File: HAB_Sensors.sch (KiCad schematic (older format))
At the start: 17 parts, among them U6 MCP9808T, U7 BME280, U8 LM4030, U9 LSM9DS1

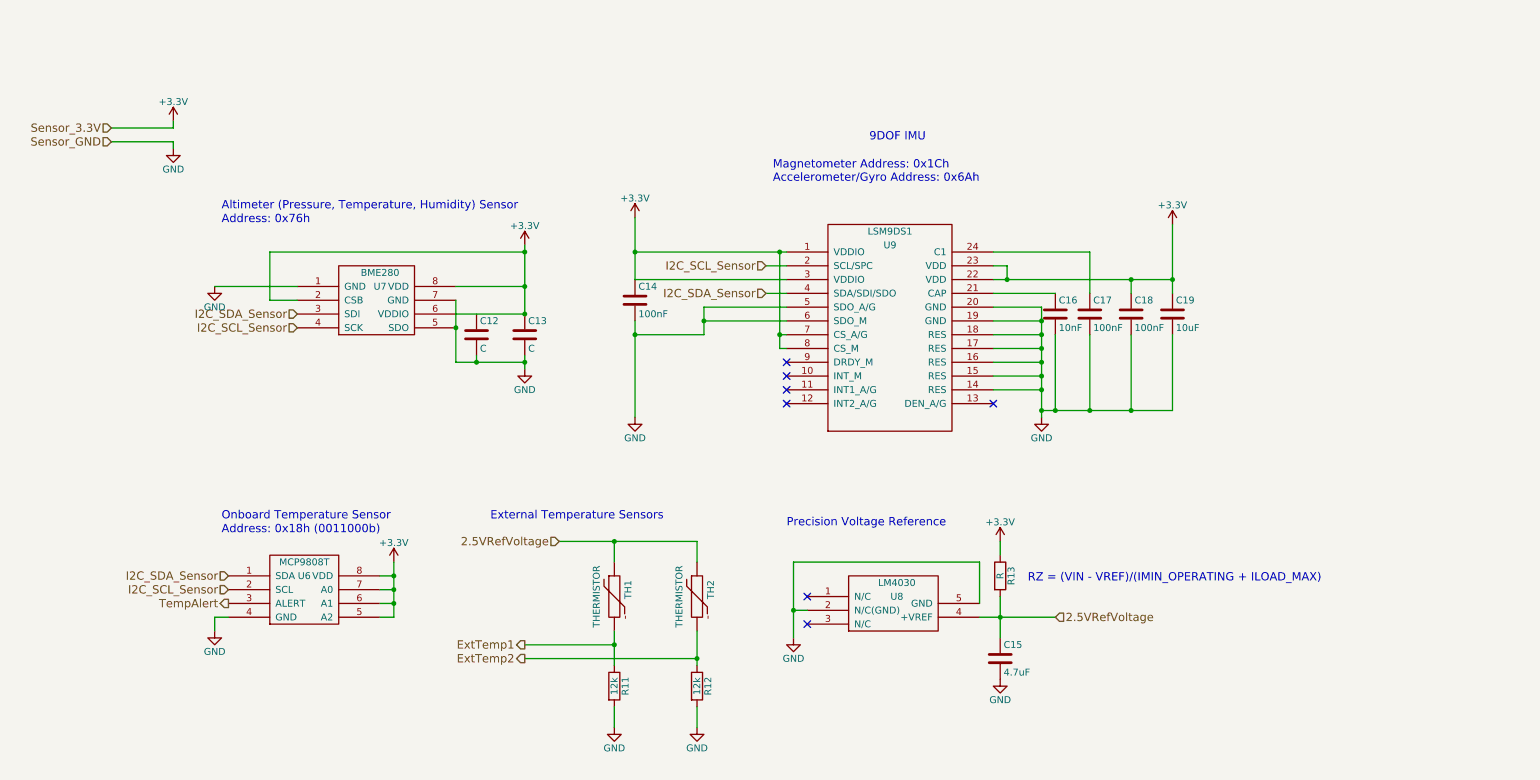
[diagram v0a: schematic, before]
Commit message: added add'l temperature sensor
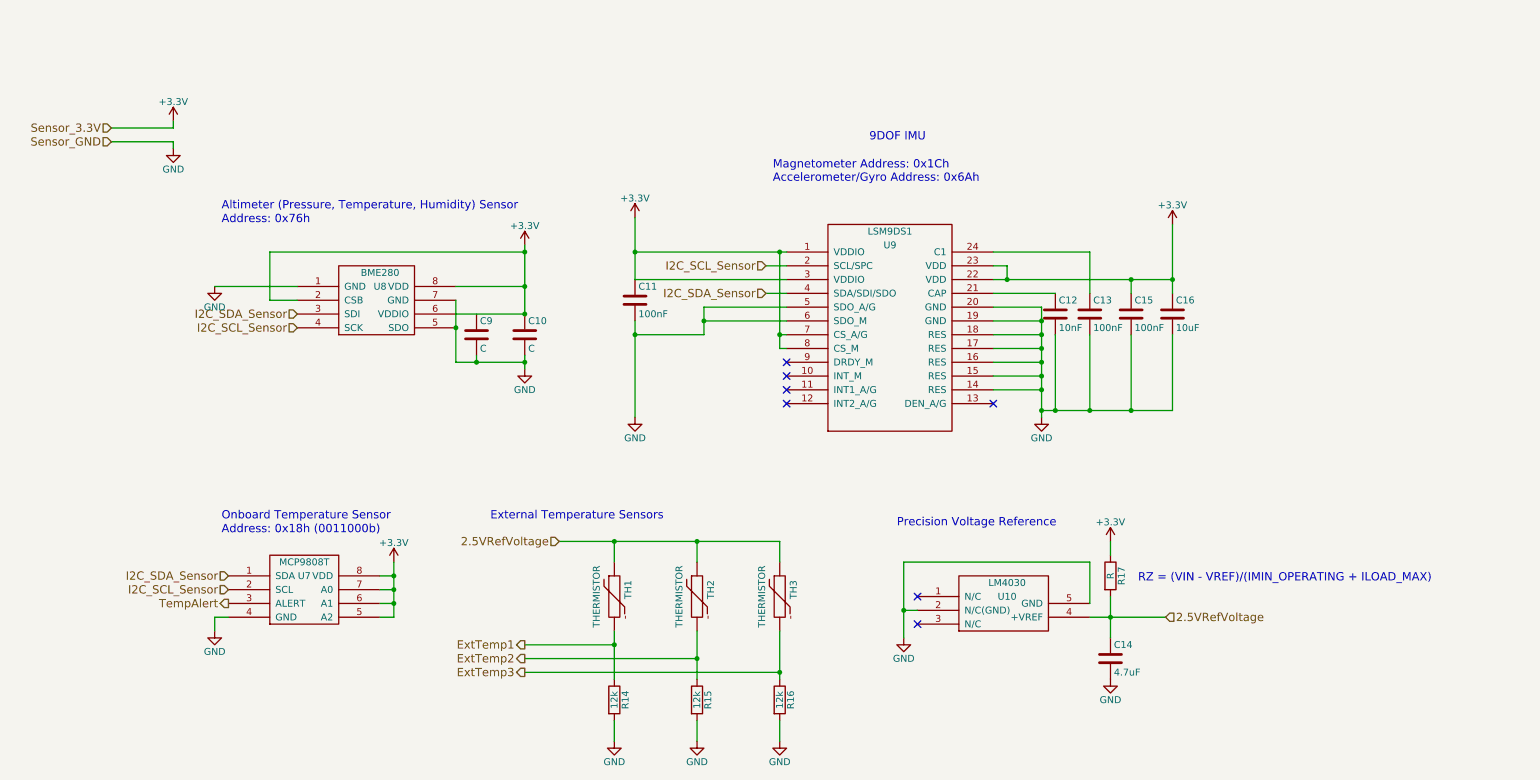
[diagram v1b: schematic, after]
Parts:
- added R15: 12k, symbol R
- added TH3: THERMISTOR, symbol THERMISTOR
- renumbered C13 to C10, C14 to C11, C16 to C12, C17 to C13, C15 to C14, C18 to C15, C19 to C16, C12 to C9, R11 to R14, R12 to R16, R13 to R17, U8 to U10, U6 to U7, U7 to U8
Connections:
- net 2.5VRefVoltage: now also TH3.1
- net ExtTemp2: now also R15.1; no longer R16.1
- net GND: now also R15.2
- new net ExtTemp3: R16.1, TH3.2
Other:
- moved on the sheet: C14, R14, R16, R17, U10

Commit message: Schematics updated/components generated/PCB started
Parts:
- C10, C11, C12, C13, C14, C15, C16, C9: footprint (none) -> Capacitors_SMD:C_0603
- R14, R15, R16, R17: footprint (none) -> Resistors_SMD:R_0603
- TH1, TH2, TH3: footprint (none) -> Connect:PINHEAD1-2
- U10: footprint MODULE -> TO_SOT_Packages_SMD:SOT-23-5
- U7: footprint MODULE -> Housings_SSOP:MSOP-8_3x3mm_Pitch0.65mm
- U8: footprint MODULE -> SPEX_Parts:LGA-8
- U9: footprint MODULE -> SPEX_Parts:LGA-24
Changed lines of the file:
@@
 LIBS:parts
 LIBS:PRESSURE-BMP180_LGA7_
+LIBS:74xgxx
+LIBS:ac-dc
+LIBS:actel
+LIBS:Altera
+LIBS:analog_devices
+LIBS:brooktre
+LIBS:cmos_ieee
+LIBS:dc-dc
+LIBS:diode
+LIBS:elec-unifil
+LIBS:ESD_Protection
+LIBS:ftdi
+LIBS:gennum
+LIBS:graphic
+LIBS:hc11
+LIBS:ir
+LIBS:Lattice
+LIBS:logo
+LIBS:maxim
+LIBS:microchip_dspic33dsc
+LIBS:microchip_pic10mcu
+LIBS:microchip_pic12mcu
+LIBS:microchip_pic16mcu
+LIBS:microchip_pic18mcu
+LIBS:microchip_pic32mcu
+LIBS:motor_drivers
+LIBS:msp430
+LIBS:nordicsemi
+LIBS:nxp_armmcu
+LIBS:onsemi
+LIBS:Oscillators
+LIBS:Power_Management
+LIBS:powerint
+LIBS:pspice
+LIBS:references
+LIBS:relays
+LIBS:rfcom
+LIBS:sensors
+LIBS:silabs
+LIBS:stm8
+LIBS:stm32
+LIBS:supertex
+LIBS:switches
+LIBS:transf
+LIBS:ttl_ieee
+LIBS:video
+LIBS:Xicor
+LIBS:Zilog
 LIBS:Spex-Mainboard-Hardware-cache
 EELAYER 25 0
@@
 F 0 "U9" H 6900 3100 50  0000 C CNN
 F 1 "LSM9DS1" H 6900 3200 50  0000 C CNN
-F 2 "MODULE" H 7050 1800 50  0001 C CNN
+F 2 "SPEX_Parts:LGA-24" H 7050 1800 50  0001 C CNN
 F 3 "DOCUMENTATION" H 7050 1800 50  0001 C CNN
 	1    6900 2500
@@
 F 0 "U7" H 2650 4600 50  0000 C CNN
 F 1 "MCP9808T" H 2650 4700 50  0000 C CNN
-F 2 "MODULE" H 2750 3950 50  0001 C CNN
+F 2 "Housings_SSOP:MSOP-8_3x3mm_Pitch0.65mm" H 2750 3950 50  0001 C CNN
 F 3 "DOCUMENTATION" H 2600 4050 50  0001 C CNN
 	1    2450 4450
@@
 F 0 "U8" H 3200 2500 50  0000 C CNN
 F 1 "BME280" H 3200 2600 50  0000 C CNN
-F 2 "MODULE" H 3300 1950 50  0001 C CNN
+F 2 "SPEX_Parts:LGA-8" H 3300 1950 50  0001 C CNN
 F 3 "DOCUMENTATION" H 3150 2050 50  0001 C CNN
 	1    3000 2350
@@
 $EndComp
 $Comp
-L +3.3V #PWR032
+L +3.3V #PWR036
 U 1 1 56DF3EDE
 P 4250 1900
-F 0 "#PWR032" H 4250 1750 50  0001 C CNN
+F 0 "#PWR036" H 4250 1750 50  0001 C CNN
 F 1 "+3.3V" H 4250 2040 50  0000 C CNN
 F 2 "" H 4250 1900 50  0000 C CNN
@@
 $EndComp
 $Comp
-L +3.3V #PWR033
+L +3.3V #PWR037
 U 1 1 56DF3EFC
 P 3300 4200
-F 0 "#PWR033" H 3300 4050 50  0001 C CNN
+F 0 "#PWR037" H 3300 4050 50  0001 C CNN
 F 1 "+3.3V" H 3300 4340 50  0000 C CNN
 F 2 "" H 3300 4200 50  0000 C CNN
@@
 $EndComp
 $Comp
-L +3.3V #PWR034
+L +3.3V #PWR038
 U 1 1 56DF3F1A
 P 8950 1750
-F 0 "#PWR034" H 8950 1600 50  0001 C CNN
+F 0 "#PWR038" H 8950 1600 50  0001 C CNN
 F 1 "+3.3V" H 8950 1890 50  0000 C CNN
 F 2 "" H 8950 1750 50  0000 C CNN
@@
 $EndComp
 $Comp
-L +3.3V #PWR035
+L +3.3V #PWR039
 U 1 1 56DF3F56
 P 5050 1700
-F 0 "#PWR035" H 5050 1550 50  0001 C CNN
+F 0 "#PWR039" H 5050 1550 50  0001 C CNN
 F 1 "+3.3V" H 5050 1840 50  0000 C CNN
 F 2 "" H 5050 1700 50  0000 C CNN
@@
 $EndComp
 $Comp
-L GND #PWR036
+L GND #PWR040
 U 1 1 56DF3F74
 P 4250 2800
-F 0 "#PWR036" H 4250 2550 50  0001 C CNN
+F 0 "#PWR040" H 4250 2550 50  0001 C CNN
 F 1 "GND" H 4250 2650 50  0000 C CNN
 F 2 "" H 4250 2800 50  0000 C CNN
@@
 $EndComp
 $Comp
-L GND #PWR037
+L GND #PWR041
 U 1 1 56DF3F92
 P 2000 2200
-F 0 "#PWR037" H 2000 1950 50  0001 C CNN
+F 0 "#PWR041" H 2000 1950 50  0001 C CNN
 F 1 "GND" H 2000 2050 50  0000 C CNN
 F 2 "" H 2000 2200 50  0000 C CNN
@@
 $EndComp
 $Comp
-L GND #PWR038
+L GND #PWR042
 U 1 1 56DF3FCE
 P 2000 4700
-F 0 "#PWR038" H 2000 4450 50  0001 C CNN
+F 0 "#PWR042" H 2000 4450 50  0001 C CNN
 F 1 "GND" H 2000 4550 50  0000 C CNN
 F 2 "" H 2000 4700 50  0000 C CNN
@@
 $EndComp
 $Comp
-L GND #PWR039
+L GND #PWR043
 U 1 1 56DF3FEC
 P 8000 3150
-F 0 "#PWR039" H 8000 2900 50  0001 C CNN
+F 0 "#PWR043" H 8000 2900 50  0001 C CNN
 F 1 "GND" H 8000 3000 50  0000 C CNN
 F 2 "" H 8000 3150 50  0000 C CNN
@@
 F 0 "C10" H 4275 2650 50  0000 L CNN
 F 1 "C" H 4275 2450 50  0000 L CNN
-F 2 "" H 4288 2400 50  0000 C CNN
+F 2 "Capacitors_SMD:C_0603" H 4288 2400 50  0001 C CNN
 F 3 "" H 4250 2550 50  0000 C CNN
 	1    4250 2550
@@
 F 0 "C9" H 3925 2650 50  0000 L CNN
 F 1 "C" H 3925 2450 50  0000 L CNN
-F 2 "" H 3938 2400 50  0000 C CNN
+F 2 "Capacitors_SMD:C_0603" H 3938 2400 50  0001 C CNN
 F 3 "" H 3900 2550 50  0000 C CNN
 	1    3900 2550
@@
 F 0 "C11" H 5075 2400 50  0000 L CNN
 F 1 "100nF" H 5075 2200 50  0000 L CNN
-F 2 "" H 5088 2150 50  0000 C CNN
+F 2 "Capacitors_SMD:C_0603" H 5088 2150 50  0001 C CNN
 F 3 "" H 5050 2300 50  0000 C CNN
 	1    5050 2300
@@
 F 0 "C12" H 8125 2500 50  0000 L CNN
 F 1 "10nF" H 8125 2300 50  0000 L CNN
-F 2 "" H 8138 2250 50  0000 C CNN
+F 2 "Capacitors_SMD:C_0603" H 8138 2250 50  0001 C CNN
 F 3 "" H 8100 2400 50  0000 C CNN
 	1    8100 2400
@@
 F 0 "C13" H 8375 2500 50  0000 L CNN
 F 1 "100nF" H 8375 2300 50  0000 L CNN
-F 2 "" H 8388 2250 50  0000 C CNN
+F 2 "Capacitors_SMD:C_0603" H 8388 2250 50  0001 C CNN
 F 3 "" H 8350 2400 50  0000 C CNN
 	1    8350 2400
@@
 F 0 "C15" H 8675 2500 50  0000 L CNN
 F 1 "100nF" H 8675 2300 50  0000 L CNN
-F 2 "" H 8688 2250 50  0000 C CNN
+F 2 "Capacitors_SMD:C_0603" H 8688 2250 50  0001 C CNN
 F 3 "" H 8650 2400 50  0000 C CNN
 	1    8650 2400
@@
 F 0 "C16" H 8975 2500 50  0000 L CNN
 F 1 "10uF" H 8975 2300 50  0000 L CNN
-F 2 "" H 8988 2250 50  0000 C CNN
+F 2 "Capacitors_SMD:C_0603" H 8988 2250 50  0001 C CNN
 F 3 "" H 8950 2400 50  0000 C CNN
 	1    8950 2400
@@
 I2C_SCL_Sensor
 $Comp
-L GND #PWR040
+L GND #PWR044
 U 1 1 56DF8E0E
 P 5050 3150
-F 0 "#PWR040" H 5050 2900 50  0001 C CNN
+F 0 "#PWR044" H 5050 2900 50  0001 C CNN
 F 1 "GND" H 5050 3000 50  0000 C CNN
 F 2 "" H 5050 3150 50  0000 C CNN
@@
 F 0 "U10" H 7750 4650 50  0000 C CNN
 F 1 "LM4030" H 7750 4750 50  0000 C CNN
-F 2 "MODULE" H 7900 4150 50  0001 C CNN
+F 2 "TO_SOT_Packages_SMD:SOT-23-5" H 7900 4150 50  0001 C CNN
 F 3 "DOCUMENTATION" H 7750 4050 50  0001 C CNN
 	1    7600 4550
@@
 $EndComp
 $Comp
-L GND #PWR041
+L GND #PWR045
 U 1 1 56E7BBB4
 P 7000 4750
-F 0 "#PWR041" H 7000 4500 50  0001 C CNN
+F 0 "#PWR045" H 7000 4500 50  0001 C CNN
 F 1 "GND" H 7000 4600 50  0000 C CNN
 F 2 "" H 7000 4750 50  0000 C CNN
@@
 2.5VRefVoltage
 $Comp
-L +3.3V #PWR042
+L +3.3V #PWR046
 U 1 1 56E7C137
 P 8500 4050
-F 0 "#PWR042" H 8500 3900 50  0001 C CNN
+F 0 "#PWR046" H 8500 3900 50  0001 C CNN
 F 1 "+3.3V" H 8500 4190 50  0000 C CNN
 F 2 "" H 8500 4050 50  0000 C CNN
@@
 F 0 "R17" V 8580 4300 50  0000 C CNN
 F 1 "R" V 8500 4300 50  0000 C CNN
-F 2 "" V 8430 4300 50  0000 C CNN
+F 2 "Resistors_SMD:R_0603" V 8430 4300 50  0001 C CNN
 F 3 "" H 8500 4300 50  0000 C CNN
 	1    8500 4300
@@
 F 0 "C14" H 8525 5000 50  0000 L CNN
 F 1 "4.7uF" H 8525 4800 50  0000 L CNN
-F 2 "" H 8538 4750 50  0000 C CNN
+F 2 "Capacitors_SMD:C_0603" H 8538 4750 50  0001 C CNN
 F 3 "" H 8500 4900 50  0000 C CNN
 	1    8500 4900
@@
 Connection ~ 8500 4600
 $Comp
-L GND #PWR043
+L GND #PWR047
 U 1 1 56E7C40E
 P 8500 5050
-F 0 "#PWR043" H 8500 4800 50  0001 C CNN
+F 0 "#PWR047" H 8500 4800 50  0001 C CNN
 F 1 "GND" H 8500 4900 50  0000 C CNN
 F 2 "" H 8500 5050 50  0000 C CNN
@@
 F 0 "TH1" V 5000 4500 50  0000 C CNN
 F 1 "THERMISTOR" V 4800 4450 50  0000 C BNN
-F 2 "" H 4900 4450 50  0000 C CNN
+F 2 "Connect:PINHEAD1-2" H 4900 4450 50  0001 C CNN
 F 3 "" H 4900 4450 50  0000 C CNN
 	1    4900 4450
@@
 F 0 "TH2" V 5600 4500 50  0000 C CNN
 F 1 "THERMISTOR" V 5400 4450 50  0000 C BNN
-F 2 "" H 5500 4450 50  0000 C CNN
+F 2 "Connect:PINHEAD1-2" H 5500 4450 50  0001 C CNN
 F 3 "" H 5500 4450 50  0000 C CNN
 	1    5500 4450
@@
 F 0 "R14" V 4980 5200 50  0000 C CNN
 F 1 "12k" V 4900 5200 50  0000 C CNN
-F 2 "" V 4830 5200 50  0000 C CNN
+F 2 "Resistors_SMD:R_0603" V 4830 5200 50  0001 C CNN
 F 3 "" H 4900 5200 50  0000 C CNN
 	1    4900 5200
@@
 F 0 "R16" V 6180 5200 50  0000 C CNN
 F 1 "12k" V 6100 5200 50  0000 C CNN
-F 2 "" V 6030 5200 50  0000 C CNN
+F 2 "Resistors_SMD:R_0603" V 6030 5200 50  0001 C CNN
 F 3 "" H 6100 5200 50  0000 C CNN
 	1    6100 5200
@@
 $EndComp
 $Comp
-L GND #PWR044
+L GND #PWR048
 U 1 1 56E7CBC6
 P 4900 5500
-F 0 "#PWR044" H 4900 5250 50  0001 C CNN
+F 0 "#PWR048" H 4900 5250 50  0001 C CNN
 F 1 "GND" H 4900 5350 50  0000 C CNN
 F 2 "" H 4900 5500 50  0000 C CNN
@@
 $EndComp
 $Comp
-L GND #PWR045
+L GND #PWR049
 U 1 1 56E7CBF2
 P 6100 5500
-F 0 "#PWR045" H 6100 5250 50  0001 C CNN
+F 0 "#PWR049" H 6100 5250 50  0001 C CNN
 F 1 "GND" H 6100 5350 50  0000 C CNN
 F 2 "" H 6100 5500 50  0000 C CNN
@@
 Sensor_3.3V
 $Comp
-L +3.3V #PWR046
+L +3.3V #PWR050
 U 1 1 56E8E1D1
 P 1700 1000
-F 0 "#PWR046" H 1700 850 50  0001 C CNN
+F 0 "#PWR050" H 1700 850 50  0001 C CNN
 F 1 "+3.3V" H 1700 1140 50  0000 C CNN
 F 2 "" H 1700 1000 50  0000 C CNN
@@
 Sensor_GND
 $Comp
-L GND #PWR047
+L GND #PWR051
 U 1 1 56E8E7BD
 P 1700 1200
-F 0 "#PWR047" H 1700 950 50  0001 C CNN
+F 0 "#PWR051" H 1700 950 50  0001 C CNN
 F 1 "GND" H 1700 1050 50  0000 C CNN
 F 2 "" H 1700 1200 50  0000 C CNN
@@
 F 0 "TH3" V 6200 4500 50  0000 C CNN
 F 1 "THERMISTOR" V 6000 4450 50  0000 C BNN
-F 2 "" H 6100 4450 50  0000 C CNN
+F 2 "Connect:PINHEAD1-2" H 6100 4450 50  0001 C CNN
 F 3 "" H 6100 4450 50  0000 C CNN
 	1    6100 4450
@@
 F 0 "R15" V 5580 5200 50  0000 C CNN
 F 1 "12k" V 5500 5200 50  0000 C CNN
-F 2 "" V 5430 5200 50  0000 C CNN
+F 2 "Resistors_SMD:R_0603" V 5430 5200 50  0001 C CNN
 F 3 "" H 5500 5200 50  0000 C CNN
 	1    5500 5200
@@
 $EndComp
 $Comp
-L GND #PWR048
+L GND #PWR052
 U 1 1 56F543F0
 P 5500 5500
-F 0 "#PWR048" H 5500 5250 50  0001 C CNN
+F 0 "#PWR052" H 5500 5250 50  0001 C CNN
 F 1 "GND" H 5500 5350 50  0000 C CNN
 F 2 "" H 5500 5500 50  0000 C CNN

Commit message: schematic updated
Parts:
- added C22: C, Capacitors_SMD:C_0603, symbol C
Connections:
- net +3V3: now also C9.1, C22.1
- net GND: now also C22.2
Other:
- moved on the sheet: C9

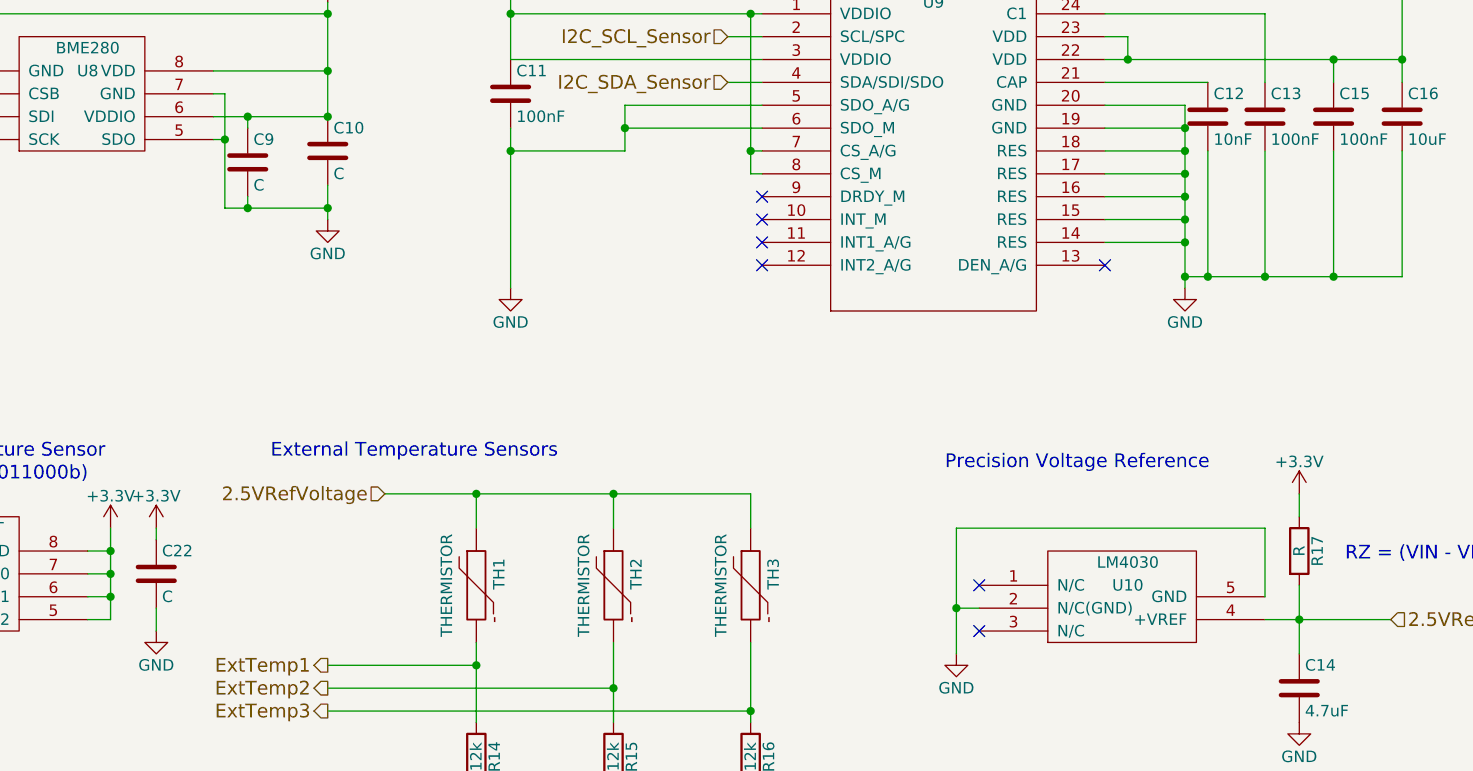
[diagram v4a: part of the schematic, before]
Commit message: updated passive values
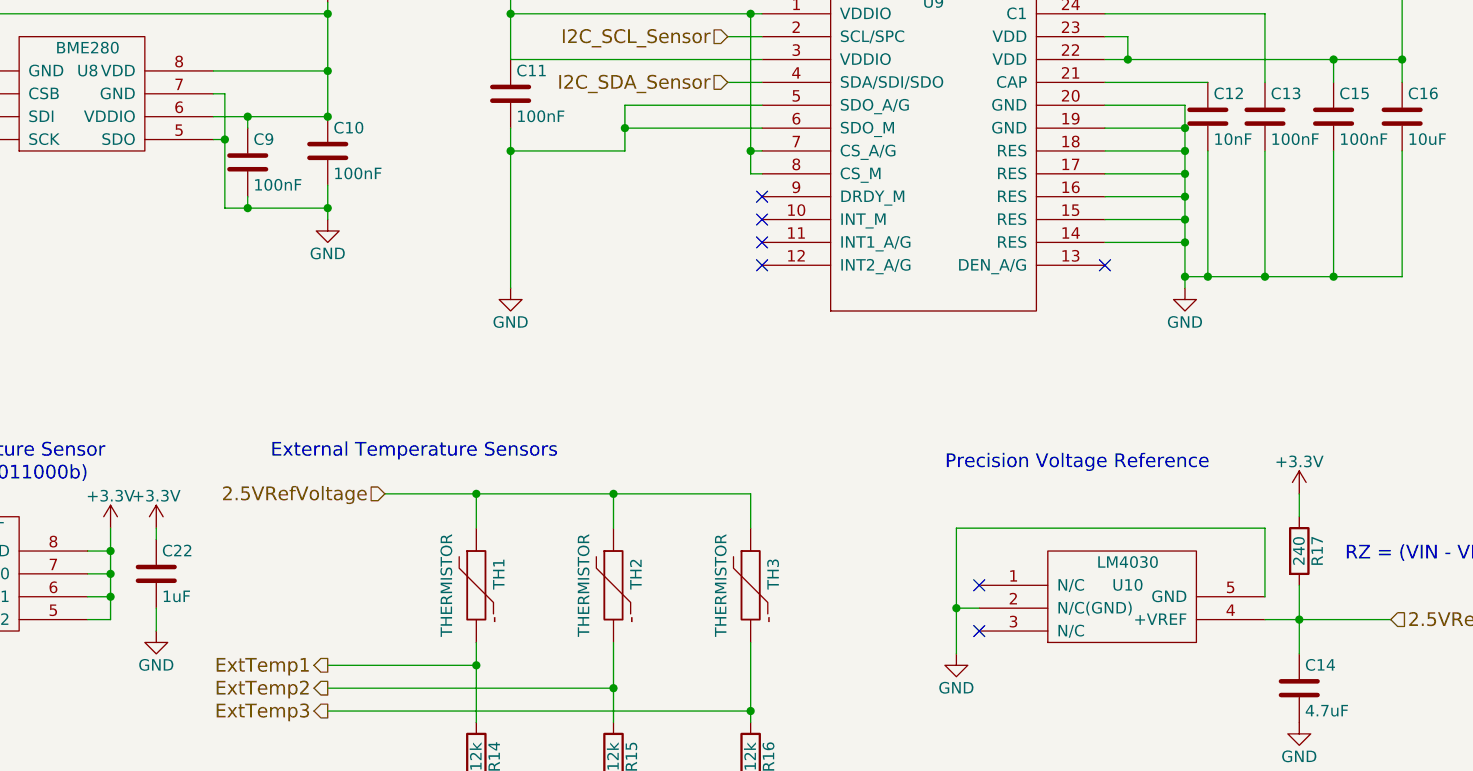
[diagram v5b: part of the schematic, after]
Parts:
- C10, C9: value C -> 100nF
- C22: value C -> 1uF
- R17: value R -> 240
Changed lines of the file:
@@
 P 4250 2550
 F 0 "C10" H 4275 2650 50  0000 L CNN
-F 1 "C" H 4275 2450 50  0000 L CNN
+F 1 "100nF" H 4275 2450 50  0000 L CNN
 F 2 "Capacitors_SMD:C_0603" H 4288 2400 50  0001 C CNN
 F 3 "" H 4250 2550 50  0000 C CNN
@@
 P 3900 2600
 F 0 "C9" H 3925 2700 50  0000 L CNN
-F 1 "C" H 3925 2500 50  0000 L CNN
+F 1 "100nF" H 3925 2500 50  0000 L CNN
 F 2 "Capacitors_SMD:C_0603" H 3938 2450 50  0001 C CNN
 F 3 "" H 3900 2600 50  0000 C CNN
@@
 P 8500 4300
 F 0 "R17" V 8580 4300 50  0000 C CNN
-F 1 "R" V 8500 4300 50  0000 C CNN
+F 1 "240" V 8500 4300 50  0000 C CNN
 F 2 "Resistors_SMD:R_0603" V 8430 4300 50  0001 C CNN
 F 3 "" H 8500 4300 50  0000 C CNN
@@
 P 3500 4400
 F 0 "C22" H 3525 4500 50  0000 L CNN
-F 1 "C" H 3525 4300 50  0000 L CNN
+F 1 "1uF" H 3525 4300 50  0000 L CNN
 F 2 "Capacitors_SMD:C_0603" H 3538 4250 50  0001 C CNN
 F 3 "" H 3500 4400 50  0000 C CNN
